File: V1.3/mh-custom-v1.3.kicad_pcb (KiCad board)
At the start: 2 copper layers, 123 parts, among them J1 Conn_01x03_Male, J10 Screw_Terminal_01x02, J11 Screw_Terminal_01x02, J12 Screw_Terminal_01x02, J13 USB_A, J14 Screw_Terminal_01x02, J3 Conn_02x19_Top_Bottom, J4 Conn_02x19_Top_Bottom, J5 Screw_Terminal_01x02, J6 Screw_Terminal_01x02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

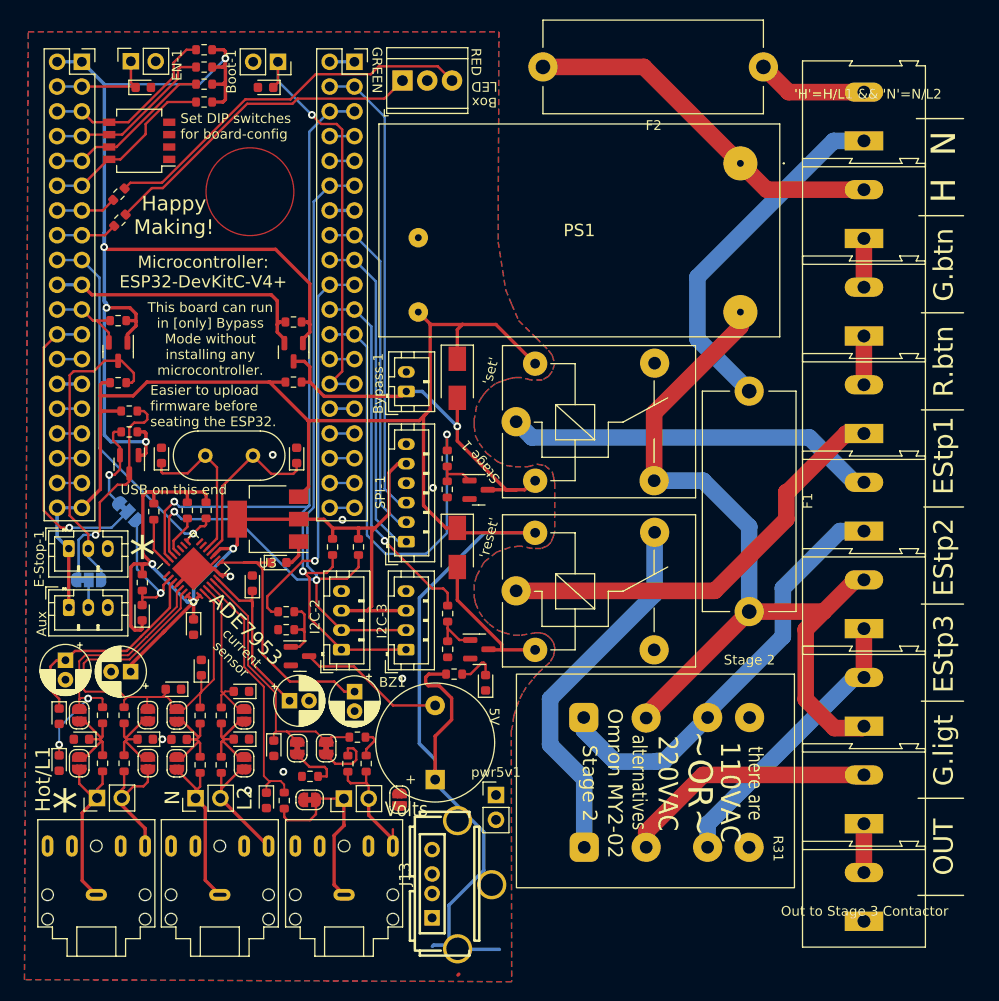
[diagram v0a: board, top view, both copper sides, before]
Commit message: rerouted to save space
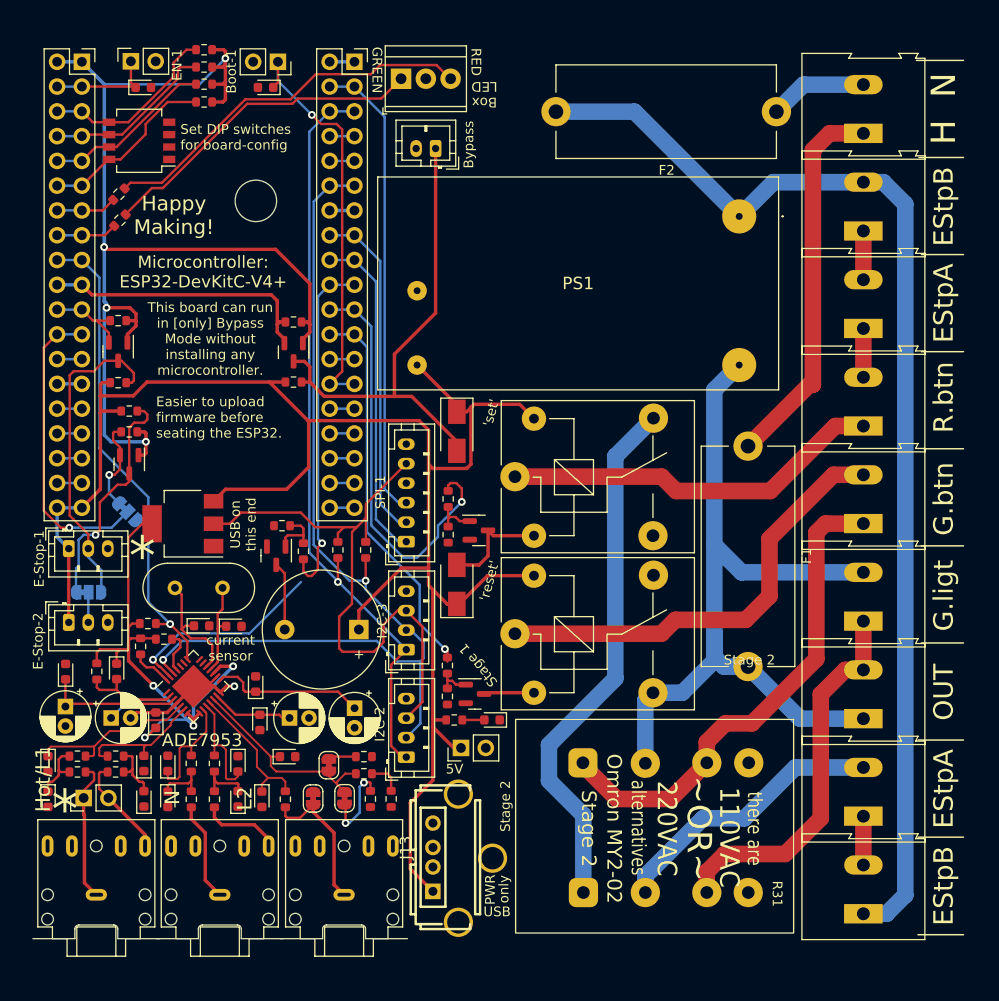
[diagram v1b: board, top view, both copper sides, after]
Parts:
- removed IN-AUX-2: N/L2, Connector_PinHeader_2.54mm:PinHeader_1x02_P2.54mm_Vertical
- removed IN-AUX-3: VOLTS, Connector_PinHeader_2.54mm:PinHeader_1x02_P2.54mm_Vertical
- removed JP1: VP-GND, Jumper:SolderJumper-2_P1.3mm_Open_RoundedPad1.0x1.5mm
- removed JP10, JP8: 48kHz-filter-1, Jumper:SolderJumper-2_P1.3mm_Open_RoundedPad1.0x1.5mm
- removed JP11, JP9: 48kHz-filter-2, Jumper:SolderJumper-2_P1.3mm_Open_RoundedPad1.0x1.5mm
- removed JP2, JP4: no-filter-1, Jumper:SolderJumper-2_P1.3mm_Open_RoundedPad1.0x1.5mm
- removed JP3, JP5: no-filter-2, Jumper:SolderJumper-2_P1.3mm_Open_RoundedPad1.0x1.5mm
- moved Bypass-1 24.4 mm to (73.2, 33.5), turned to 180 degrees
- moved relay1 21.7 mm to (82.4, 83.8)
- moved R28 21.2 mm to (75.5, 90.2)
- moved R27 21.2 mm to (75.5, 87.0)
- moved T3 20.9 mm to (78.3, 89.9)
- moved C21 18.7 mm to (53.6, 83.0), turned to 0 degrees
- moved C20 17.9 mm to (50.3, 82.9), turned to 0 degrees
- moved BZ1 16.4 mm to (62.6, 83.3), turned to 180 degrees
- moved C22 14.3 mm to (56.2, 92.8), turned to -90 degrees
- moved R24 13.9 mm to (44.0, 85.1)
- moved Y1 13.6 mm to (52.4, 79.1)
- moved R25 13.4 mm to (46.4, 84.3), turned to 180 degrees
- moved R23 13.1 mm to (44.8, 82.7), turned to 180 degrees
- moved I2C-2 12.9 mm to (71.3, 96.4)
- moved C17 12.7 mm to (55.8, 88.9), turned to 90 degrees
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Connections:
- J11 pad 1: Member-E-Stop-aux1-2 -> Member-E-Stop-aux2-2
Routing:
- net Member-E-Stop-aux2-2: track 38.4 -> 118.6 mm
- net IAN: track 50.1 -> 13.3 mm
- net +3.3V: track 102.2 -> 126.4 mm, vias 3 -> 4
- net reset: track 38.2 -> 54.5 mm
- net read-bypass: track 39.5 -> 55.2 mm, vias 1 -> 0
- net SDA: track 85.2 -> 98.7 mm
- net VP_IN: track 13.4 -> 0.68 mm
- net +5V: track 202.1 -> 189.9 mm
- net IAP: track 29.7 -> 17.9 mm, vias 2 -> 0
- net IBP: track 0.00 -> 11.8 mm
- net VN: track 26.4 -> 14.7 mm
- net Net-(C17-Pad1): track 27.2 -> 15.7 mm
- net Green-Indicator-light-2: track 29.6 -> 40.2 mm
- net ade7953-IRQ: track 39.3 -> 49.5 mm
- net Net-(C22-Pad1): track 17.9 -> 8.39 mm
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- removed copper zone on B.Cu, net GND
- removed copper zone on F.Cu, net GND
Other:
- board outline added: 13 x 1.4 mm
- board text added: "Bypass"
- board text added: "EStpA"
- board text added: "EStpB"
- board text added: "PWR"
- board text added: "USB"
- board text added: "only"
- board text removed: "'H'=H/L1 && 'N'=N/L2"
- board text removed: "Aux"
- board text removed: "EStp1"
- board text removed: "EStp2"
- board text removed: "EStp3"
- board text removed: "Out to Stage 3 Contactor"
- board text removed: "Volts"

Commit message: jumpers added to bottom
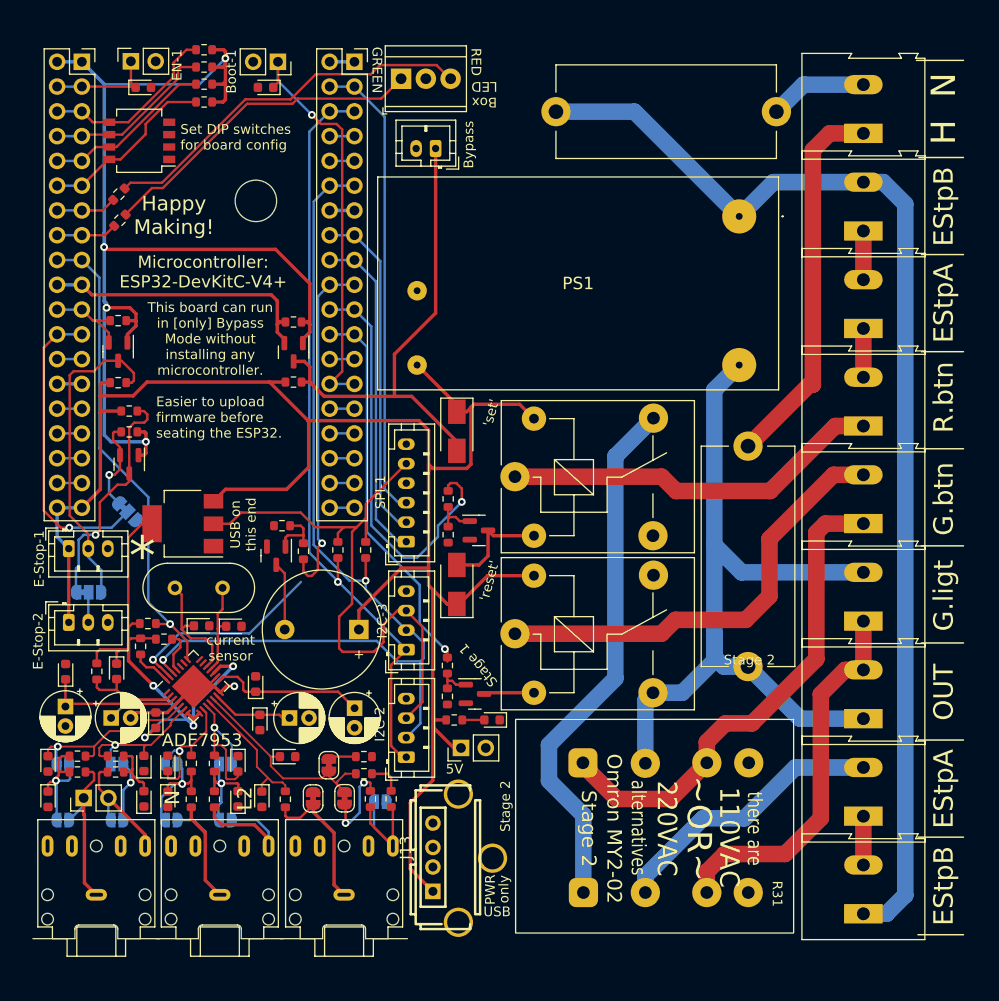
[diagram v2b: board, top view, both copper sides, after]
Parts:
- added JP1: no-filter-1, Jumper:SolderJumper-2_P1.3mm_Open_RoundedPad1.0x1.5mm, B.Cu at (68.6, 101.0)
- added JP10: no-filter-1, Jumper:SolderJumper-2_P1.3mm_Open_RoundedPad1.0x1.5mm, B.Cu at (47.2, 97.1)
- added JP11: no-filter-1, Jumper:SolderJumper-2_P1.3mm_Open_RoundedPad1.0x1.5mm, B.Cu at (52.7, 97.1)
- added JP2: no-filter-1, Jumper:SolderJumper-2_P1.3mm_Open_RoundedPad1.0x1.5mm, B.Cu at (36.1, 102.9)
- added JP3: no-filter-1, Jumper:SolderJumper-2_P1.3mm_Open_RoundedPad1.0x1.5mm, B.Cu at (41.6, 102.9)
- added JP4: no-filter-1, Jumper:SolderJumper-2_P1.3mm_Open_RoundedPad1.0x1.5mm, B.Cu at (47.2, 102.9)
- added JP5: no-filter-1, Jumper:SolderJumper-2_P1.3mm_Open_RoundedPad1.0x1.5mm, B.Cu at (52.7, 102.9)
- added JP8: no-filter-1, Jumper:SolderJumper-2_P1.3mm_Open_RoundedPad1.0x1.5mm, B.Cu at (36.1, 97.1)
- added JP9: no-filter-1, Jumper:SolderJumper-2_P1.3mm_Open_RoundedPad1.0x1.5mm, B.Cu at (41.6, 97.1)
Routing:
- net VP_IN: track 0.68 -> 15.1 mm
- net IBP_IN: track 10.2 -> 20.6 mm
- net Net-(C3-Pad1): track 6.28 -> 13.9 mm, vias 0 -> 1
- net Net-(C5-Pad1): track 5.27 -> 12.9 mm, vias 0 -> 1
- net Net-(C4-Pad2): track 6.14 -> 13.4 mm, vias 0 -> 1
- net Net-(C6-Pad2): track 5.54 -> 11.5 mm, vias 0 -> 1
- net IBN_IN: track 8.27 -> 14.0 mm
- net IBN: track 11.6 -> 16.0 mm, vias 0 -> 1
- net IAP_IN: track 14.4 -> 17.2 mm
- net IBP: track 11.8 -> 14.1 mm, vias 0 -> 1
- net IAN_IN: track 10.3 -> 12.7 mm
- net IAN: track 13.3 -> 15.4 mm, vias 0 -> 1
- net IAP: track 17.9 -> 19.7 mm, vias 0 -> 1
- net VP: track 21.7 -> 22.3 mm
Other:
- board text added: "HOT/L1"
- board text added: "Hardware: V1.3.0"
- board text added: "Set DIP switches for board config"
- board text added: "Vincent, Lior, J.R., Chris, and Ashley"
- board text removed: "Hardware: V1.2.0"
- board text removed: "Hot/L1"
- board text removed: "Set DIP switches for board-config"
- board text removed: "Vincent, Lior, J.R., & Chris"

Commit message: fixing edges and connecting all pieces
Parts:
- moved R1 6.98 mm to (60.2, 68.3)
- moved R2 6.98 mm to (58.0, 65.7)
- moved T1 6.98 mm to (57.4, 68.8)
- moved C22 6.39 mm to (55.7, 86.5), turned to 0 degrees
- moved C17 5.11 mm to (55.5, 83.8)
- moved U3 4.66 mm to (50.2, 68.2)
- moved C21 4.22 mm to (53.6, 78.8)
- moved C20 4.22 mm to (50.3, 78.7)
- moved R23 4.22 mm to (44.8, 78.5)
- moved R24 4.22 mm to (44.0, 80.8)
- moved R25 4.22 mm to (46.4, 80.1)
- moved U2 4.22 mm to (49.4, 84.9)
- moved Y1 4.22 mm to (52.4, 74.8)
- moved C13 4.21 mm to (45.7, 88.4)
- moved R13 3.38 mm to (68.2, 97.7)
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- renumbered E-Stop-1 to EStpA, E-Stop-2 to EStpB
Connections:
- J10 pad 2: Member-E-Stop-sw1-1 -> Member-E-Stop-aux2-2
- J11 pad 1: Member-E-Stop-aux2-2 -> Member-E-Stop-sw1-1
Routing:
- net read-bypass: track 55.2 -> 93.2 mm, vias 0 -> 1
- net Member-E-Stop-aux2-2: track 118.6 -> 104.0 mm
- net Net-(C15-Pad2): track 10.1 -> 24.5 mm, vias 0 -> 1
- net SCL: track 98.7 -> 108.0 mm
- net Green-Indicator-light-2: track 40.2 -> 31.3 mm
- net +5V: track 189.9 -> 181.6 mm
- net Net-(JP14-Pad1): track 24.2 -> 18.8 mm
- net GND: track 22.9 -> 17.5 mm
- net reset3v: track 43.0 -> 37.7 mm
- net /microcontroller/lightsounds/dcp1: track 6.99 -> 11.7 mm, vias 0 -> 1
- net Member-E-Stop-sw1-1: track 28.7 -> 24.3 mm
- net ade7953-IRQ: track 49.5 -> 45.2 mm
- net +3.3V: track 126.4 -> 130.3 mm
- net buzz: track 35.8 -> 32.2 mm
- net SDA: track 98.7 -> 102.2 mm
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- added copper zone on B.Cu, net GND
- added copper zone on F.Cu, net GND
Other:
- board size 13 x 1.4 mm -> 97 x 93 mm
- board text added: "4A Fuses 5x20mm"
- board text added: "H·L1"
- board text added: "I2C"
- board text added: "NEU/L2"
- board text added: "Volts"
- board text added: "current"
- board text removed: "G.btn"
- board text removed: "G.ligt"
- board text removed: "L2"
- board text removed: "current sensor"
- board text removed: "makehaven.org/toolauth"

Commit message: connections made, style points added. needs double-check
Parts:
- moved Bypass-1 10.4 mm to (80.9, 26.5), turned to 90 degrees
- moved F1 3.19 mm to (106.2, 72.8)
- moved D2 1.50 mm to (80.0, 91.1)
- moved D3 1.50 mm to (76.4, 61.5)
- moved D4 1.50 mm to (76.4, 77.2)
- moved I2C-2 1.50 mm to (71.2, 94.9)
- moved I2C-3 1.50 mm to (71.2, 83.9)
- moved J13 1.50 mm to (75.9, 105.2)
- moved R26 1.50 mm to (76.1, 91.1)
- moved R27 1.50 mm to (75.4, 85.5)
- moved R28 1.50 mm to (75.4, 88.7)
- moved R29 1.50 mm to (75.5, 68.4)
- moved T4 1.50 mm to (78.7, 71.7)
- moved R30 1.50 mm to (75.5, 72.1)
- moved SPI-1 1.50 mm to (71.2, 72.8)
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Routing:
- net read-bypass: track 93.2 -> 102.3 mm
- net Green-Indicator-light-1: track 84.6 -> 91.9 mm
- net SDA: track 102.2 -> 96.3 mm
- net VP_IN: track 16.0 -> 10.7 mm
- net Net-(R13-Pad1): track 2.89 -> 8.27 mm
- net Green-Indicator-light-2: track 31.3 -> 35.3 mm
- net reset3v: track 37.7 -> 41.1 mm
- net H/L1: track 39.2 -> 36.5 mm
- net Member-E-Stop-aux2-2: track 104.0 -> 106.1 mm
- net +3.3V: track 130.3 -> 132.3 mm
- net set3v: track 40.1 -> 38.6 mm
- net Member-Red-Reset-Button-1: track 39.1 -> 37.7 mm
- net Member-Green-Button-2: track 48.9 -> 47.6 mm
- net +5V: track 181.6 -> 182.3 mm
- net PICO: track 47.1 -> 46.4 mm
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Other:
- board size 97 x 93 mm -> 97 x 91.3 mm
- board text added: "3 stages of relays ESP32 WiFi microcontroller 2x E-Stop Integration Current Sensor"
- board text added: "Bypass Key Input"
- board text added: "G.btn"
- board text added: "G.lght"
- board text added: "GND"
- board text added: "H N"
- board text added: "Hardware:"
- board text added: "MAX4A Fuse"
- board text added: "MAX4A Fuses 5x20mm"
- board text added: "USB PWR No Data"
- board text added: "V1.3.0"
- board text added: "for daughter boards only"
- board text added: "makehaven.org/toolauth"
- board text added: "sensor"
- board text removed: "3 stages or relays WiFi microcontroller E-Stop Integration Current Sensor"
- board text removed: "4A Fuses 5x20mm"
- board text removed: "Bypass"
- board text removed: "H"
- board text removed: "Hardware: V1.3.0"
- board text removed: "N"

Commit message: finished B silkscreen
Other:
- board text added: "Designed to use with ESPHome & Home Assistant"
- board text added: "Use at your own risk"
- board text removed: "Best when used with ESPHome & Home Assistant"

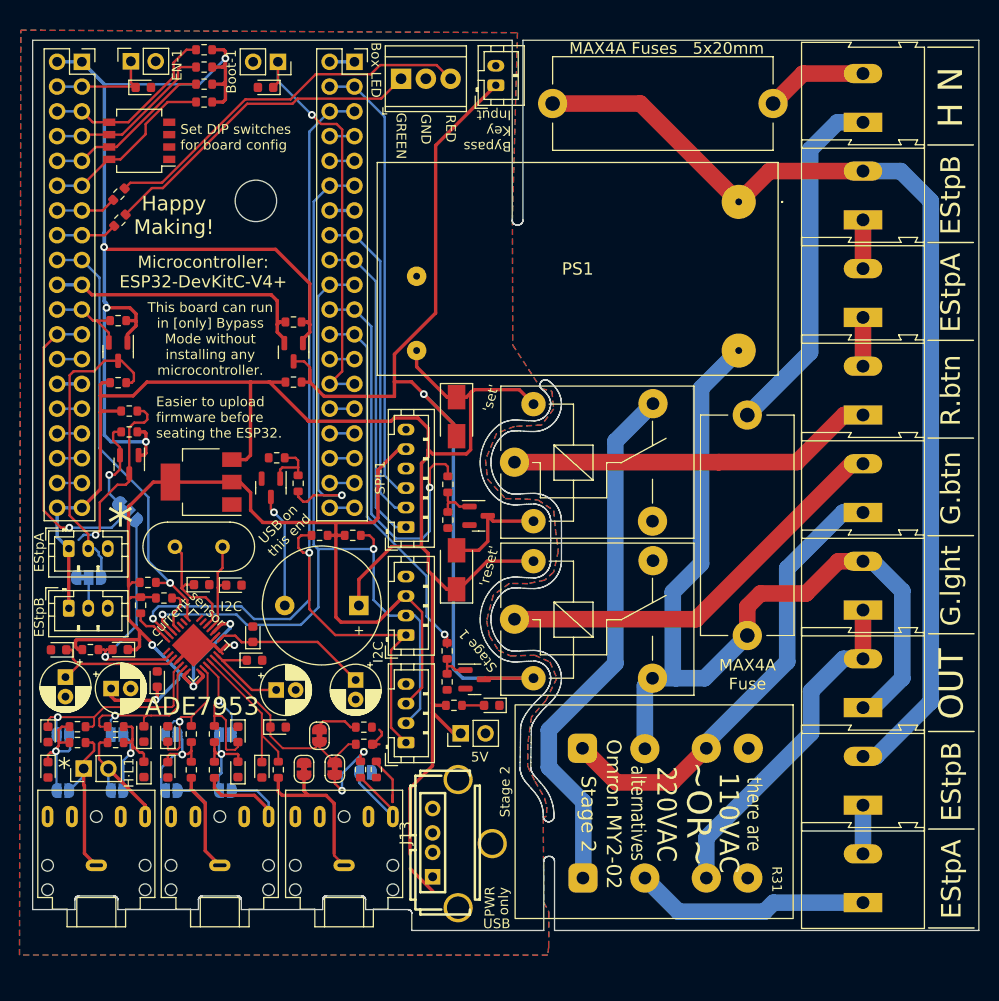
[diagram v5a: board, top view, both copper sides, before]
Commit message: minor adjustments F Silkscreen
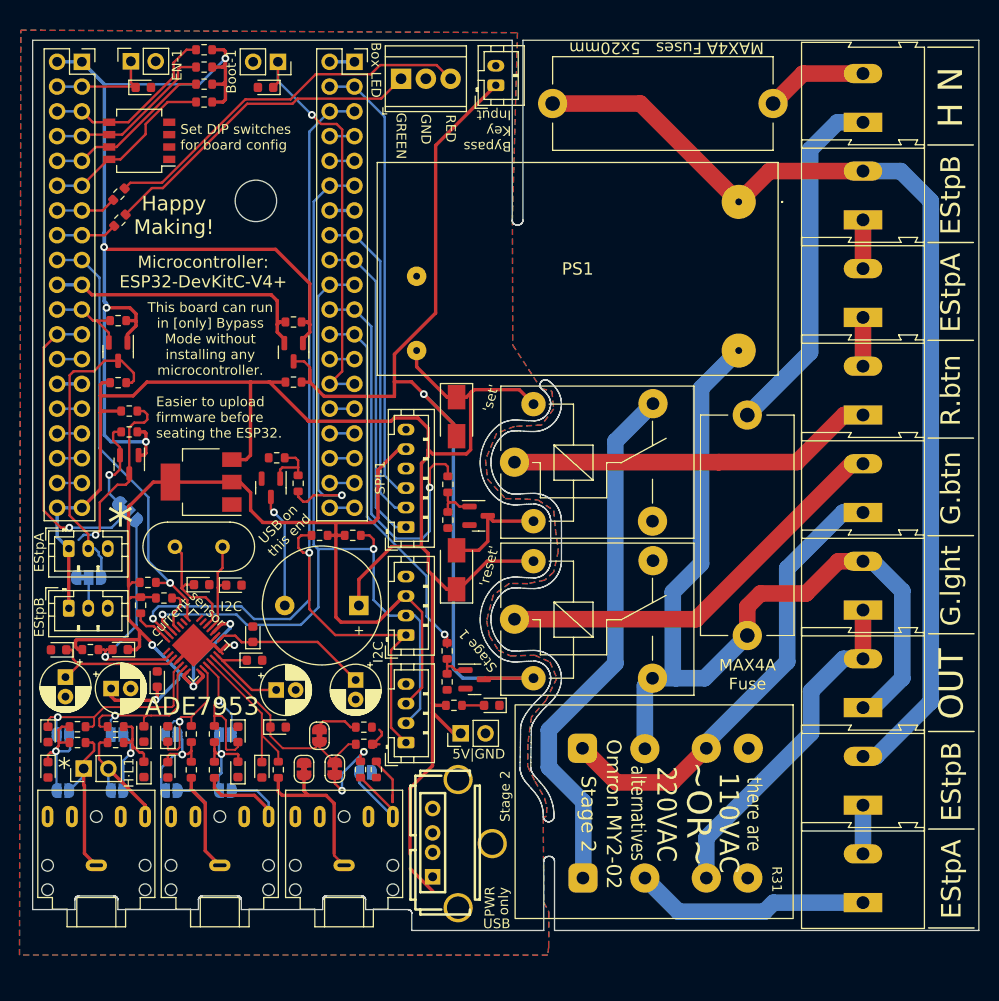
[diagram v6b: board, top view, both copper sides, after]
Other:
- board text added: "5V|GND"
- board text removed: "5V"
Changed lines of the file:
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@@
     (property "Sheetname" "breakoutboards")
     (attr through_hole)
-    (fp_text reference "J13" (at -0.254 -4.709 90) (layer "F.SilkS")
+    (fp_text reference "J13" (at -0.254 -4.709 90) (layer "F.SilkS") hide
       (effects (font (size 1.143 1.143) (thickness 0.152)) (justify left))
     )
@@
     (effects (font (size 1 1) (thickness 0.15)) (justify left))
   )
-  (gr_text "Stage 2" (at 81.3859 99.9396 90) (layer "F.SilkS")
+  (gr_text "Stage 2" (at 81.395 100.41 90) (layer "F.SilkS")
     (effects (font (size 1 1) (thickness 0.15)))
   )
@@
     (effects (font (size 1 1) (thickness 0.15)) (justify left))
   )
-  (gr_text "5V" (at 78.7855 96.3946) (layer "F.SilkS")
+  (gr_text "5V|GND" (at 78.685 96.09) (layer "F.SilkS")
     (effects (font (size 1 1) (thickness 0.15)))
   )
@@
     (effects (font (size 1 1) (thickness 0.15)) (justify left))
   )
-  (gr_text "MAX4A Fuses   5x20mm" (at 97.945 23.75) (layer "F.SilkS")
+  (gr_text "MAX4A Fuses   5x20mm" (at 97.935 23.7 180) (layer "F.SilkS")
     (effects (font (size 1.2 1.2) (thickness 0.2)))
   )
